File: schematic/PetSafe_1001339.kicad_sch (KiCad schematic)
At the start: 150 parts, among them J1 ICSP, J3 PIR BOARD, J5 MOTOR, J6 DNP, Q1 FMOS3401A?, Q11 MMBTA55?, Q2 BC847B?, Q3 MMBTA55?, Q4 MMBTA55?, Q5 MMBTA55?, Q6 MMBTA55?, Q7 BC857C?, Q8 SIL3724A?, Q9 DNP, U1 S-1200B45?, U106 U6A / DNP, U2 SN74LVC2G14DBV?, U3 SGM8542XS, U4 PIC16F18855, U5 MX512H, U6 S-812C33AMC? / 3.3V, U7 DNP, Y1 20 MHz

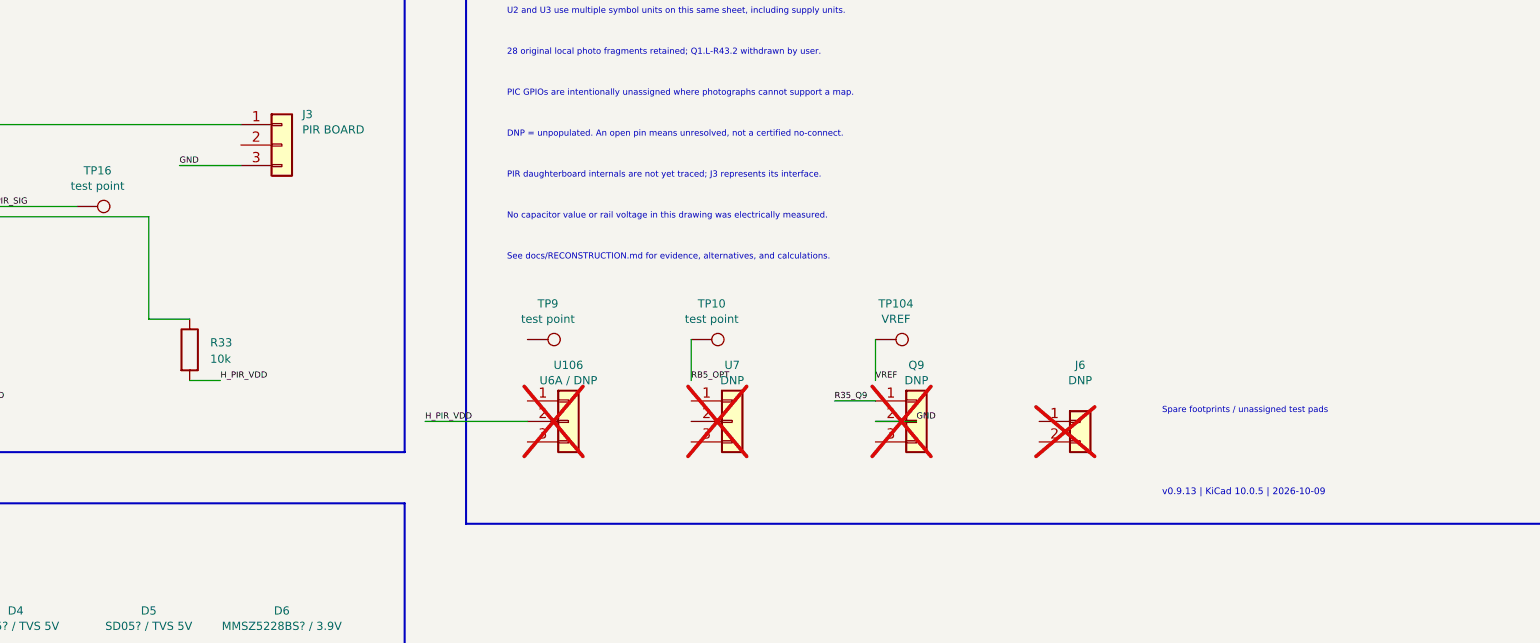
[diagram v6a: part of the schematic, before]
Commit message: Confirm J3 signal entry, R23 input and R22 ground from bench readings
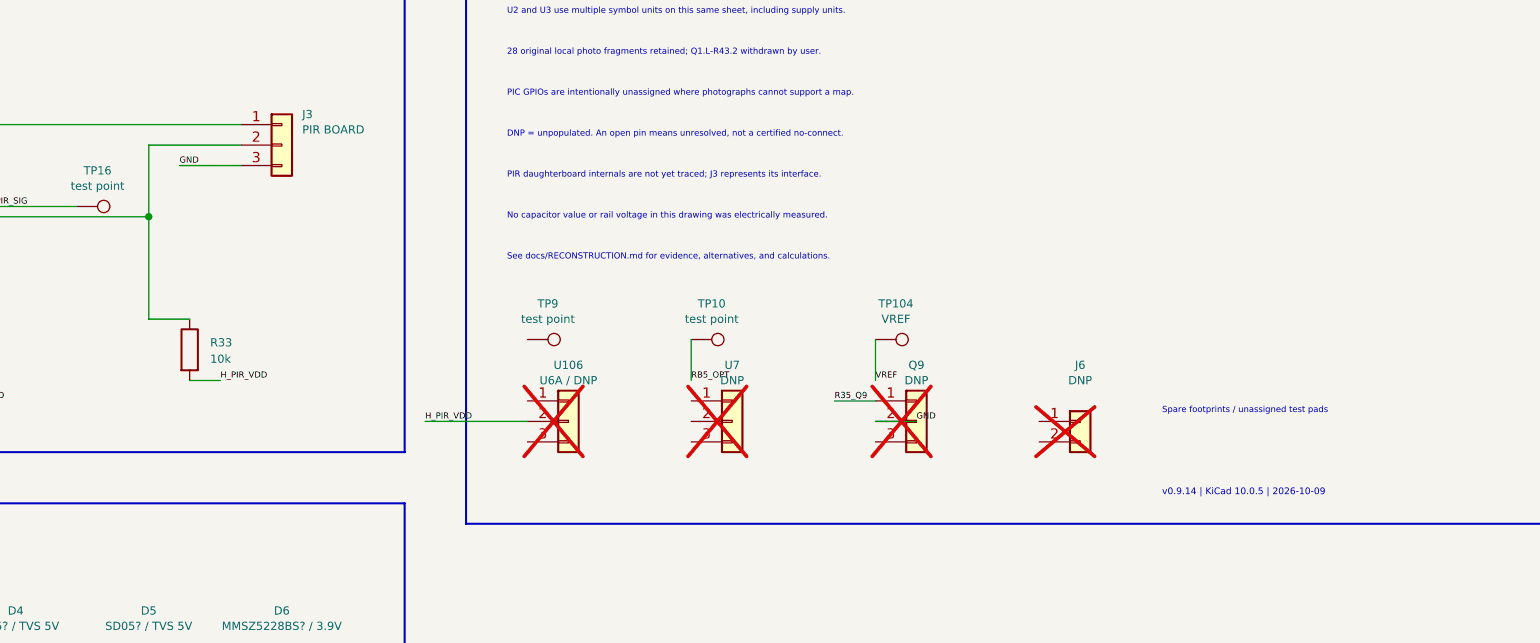
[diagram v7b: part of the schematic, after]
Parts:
- J3: MeasurementEvidence v0.9.13 user: pin3 (left / I in IMG_2435)-GND 1 ohm; pin2 (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 -> v0.9.14 user: pin1 PIR supply previously confirmed; pin2 H-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; ViaEvidence v0.9.13 user: pin3 (left / I in IMG_2435)-GND 1 ohm; pin2 (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 -> v0.9.14 user: pin1 PIR supply previously confirmed; pin2 H-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
- R22: MeasurementEvidence v0.9.13 user: D/left end in IMG_2434 is model2, U3.5/VREF a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 -> v0.9.14 user: E/right/model1-GND 1 ohm; D/left/model2-VREF 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; ViaEvidence v0.9.13 user: D/left end in IMG_2434 is model2, U3.5/VREF a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 -> v0.9.14 user: E/right/model1-GND 1 ohm; D/left/model2-VREF 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
- R23: MeasurementEvidence v0.9.13 user: both physical ends 270-289 kohm to U3.5, now 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 -> v0.9.14 user: B/left/model1-U3.6 1 ohm; C/right/model2-U3.6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; ViaEvidence v0.9.13 user: both physical ends 270-289 kohm to U3.5, now 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 -> v0.9.14 user: B/left/model1-U3.6 1 ohm; C/right/model2-U3.6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
- R38: MeasurementEvidence (none) -> v0.9.14 user: K/right/model1-J3.2 1 ohm; J/left/model2-J3.2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
- U3: MeasurementEvidence v0.9.13 user: pin5-VREF 1 ohm; pin5-R22 D/left 1 ohm, E/rig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 -> v0.9.14 user: pin5-VREF/R22 D 1 ohm (batch1); pin6-R23 B/le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
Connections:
- net at J3.2 (Pin_2): now also R33.1, R38.1
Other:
- note added: "v0.9.14 | KiCad 10.0.5 | 2026-10-09"
- note removed: "v0.9.13 | KiCad 10.0.5 | 2026-10-09"

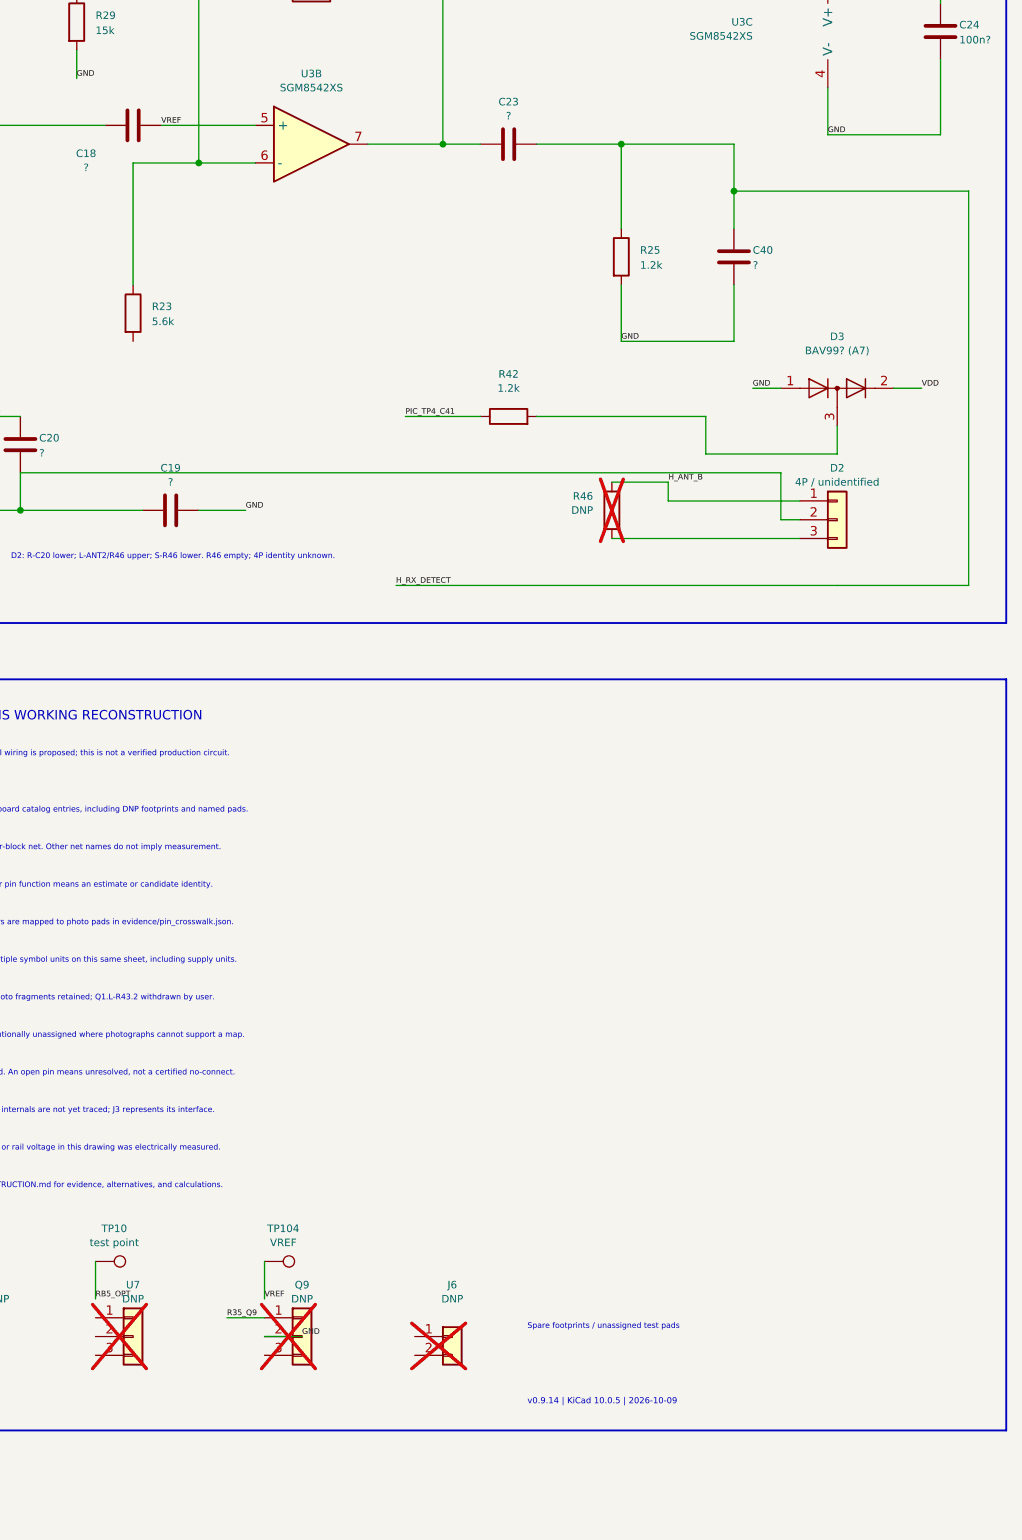
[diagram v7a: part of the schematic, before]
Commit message: Resolve R23 junction and require photo tracing before bench requests
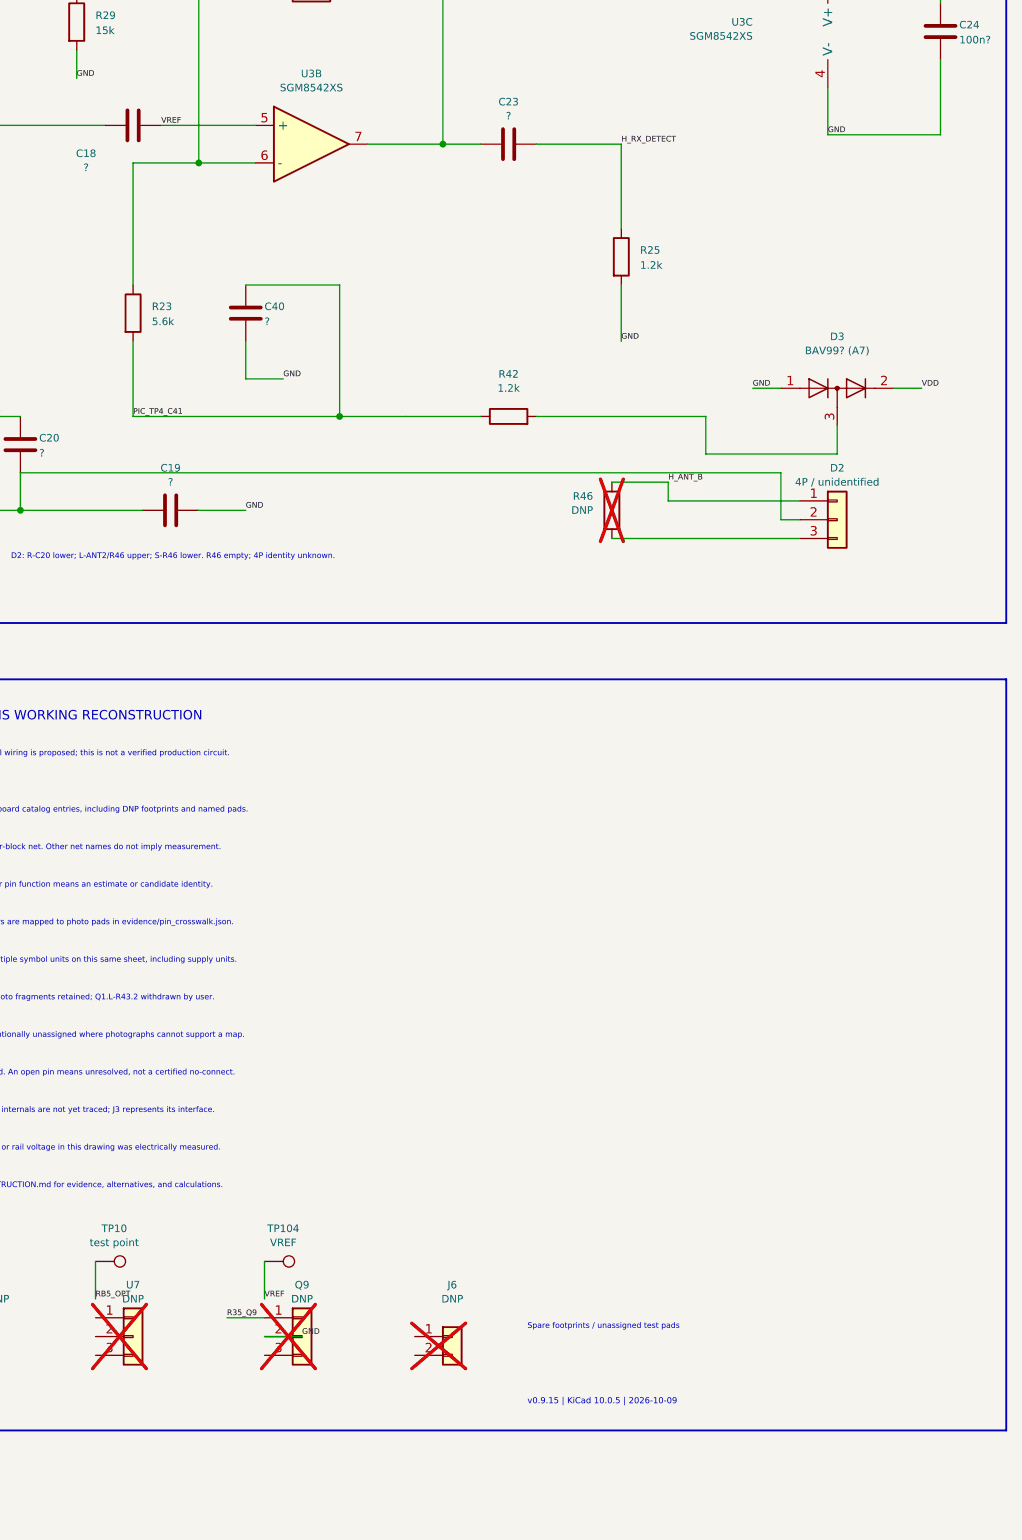
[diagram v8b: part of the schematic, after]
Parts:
- C40: MeasurementEvidence (none) -> v0.9.15: lower P/model1 joins R23 C/model2 and R42 Q/model1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; ViaEvidence v0.9.2: V083 associated with C40; earlier GND report retain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 -> v0.9.15: lower P/model1 joins R23 C/model2 and R42 Q/model1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
- R23: MeasurementEvidence v0.9.14 user: B/left/model1-U3.6 1 ohm; C/right/model2-U3.6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 -> v0.9.15: right C/model2 joins C40 lower P/model1 and R42 up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; ViaEvidence v0.9.14 user: B/left/model1-U3.6 1 ohm; C/right/model2-U3.6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 -> v0.9.15: right C/model2 joins C40 lower P/model1 and R42 up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
- R42: MeasurementEvidence (none) -> v0.9.15: upper Q/model1 joins R23 C/model2 and C40 P/model1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; ViaEvidence v0.9.8: User confirms V017-TP4. Prior V017-R42.1/R44.1 loca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 -> v0.9.15: upper Q/model1 joins R23 C/model2 and C40 P/model1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
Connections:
- net H_RX_DETECT: no longer C40.1
- net PIC_TP4_C41: now also C40.1, R23.2
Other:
- note added: "v0.9.15 | KiCad 10.0.5 | 2026-10-09"
- note removed: "v0.9.14 | KiCad 10.0.5 | 2026-10-09"
- moved on the sheet: C40
